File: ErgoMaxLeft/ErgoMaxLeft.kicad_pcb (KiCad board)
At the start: 2 copper layers, 92 parts, among them J1 AudioJack4_Ground, K1 KEYSW, K10 KEYSW, K11 KEYSW, K12 KEYSW, K13 KEYSW, K14 KEYSW, K15 KEYSW, K16 KEYSW, K17 KEYSW, K18 KEYSW, K19 KEYSW, K2 KEYSW, K20 KEYSW, K21 KEYSW, K22 KEYSW, K23 KEYSW, K24 KEYSW, K25 KEYSW, K26 KEYSW, K27 KEYSW, K28 KEYSW, K29 KEYSW, K3 KEYSW, K30 KEYSW, K31 KEYSW, K32 KEYSW, K33 KEYSW, K34 KEYSW, K35 KEYSW, K36 KEYSW, K37 KEYSW, K38 KEYSW, K39 KEYSW, K4 KEYSW, K40 KEYSW, K41 KEYSW, K42 KEYSW, K43 KEYSW, K44 KEYSW, K5 KEYSW, K6 KEYSW, K7 KEYSW, K8 KEYSW, K9 KEYSW, U1 ProMicro

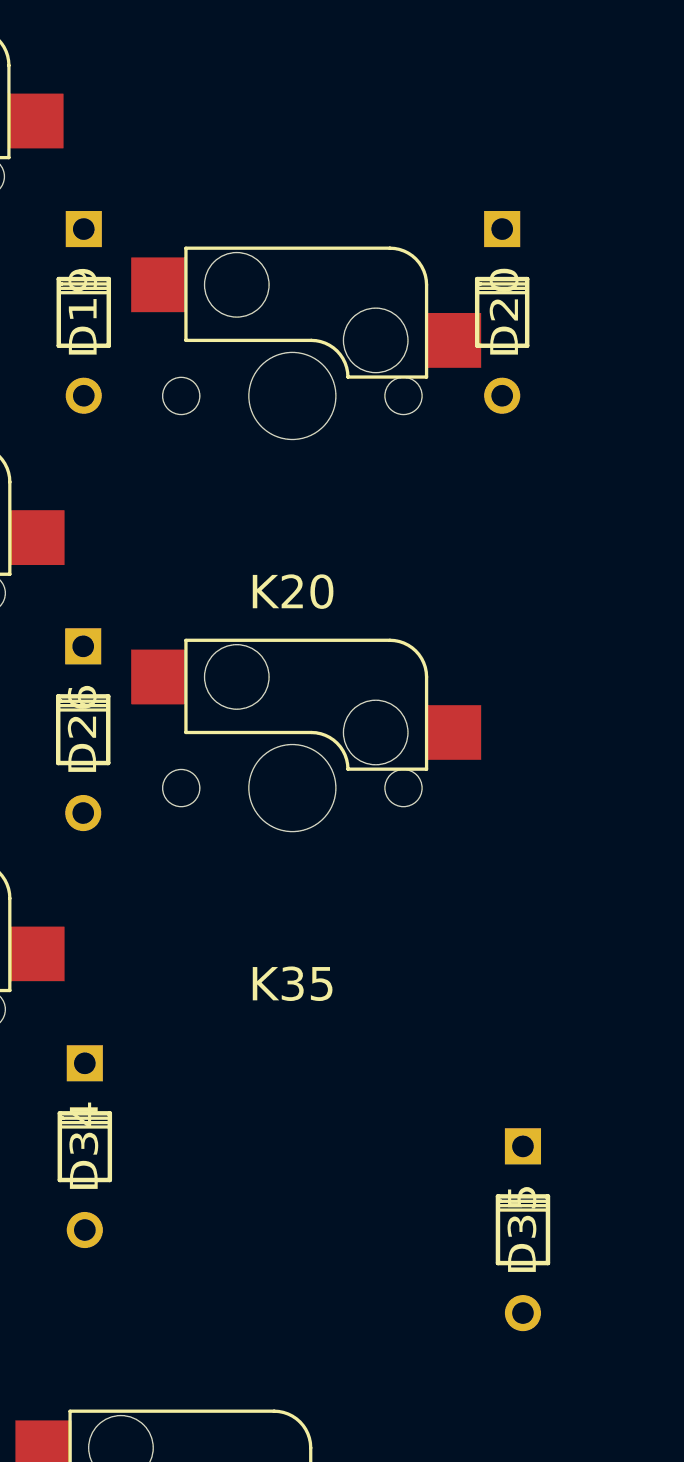
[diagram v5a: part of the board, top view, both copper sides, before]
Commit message: WIP PCB: fix spacing for the 2 1.5u keys on right side
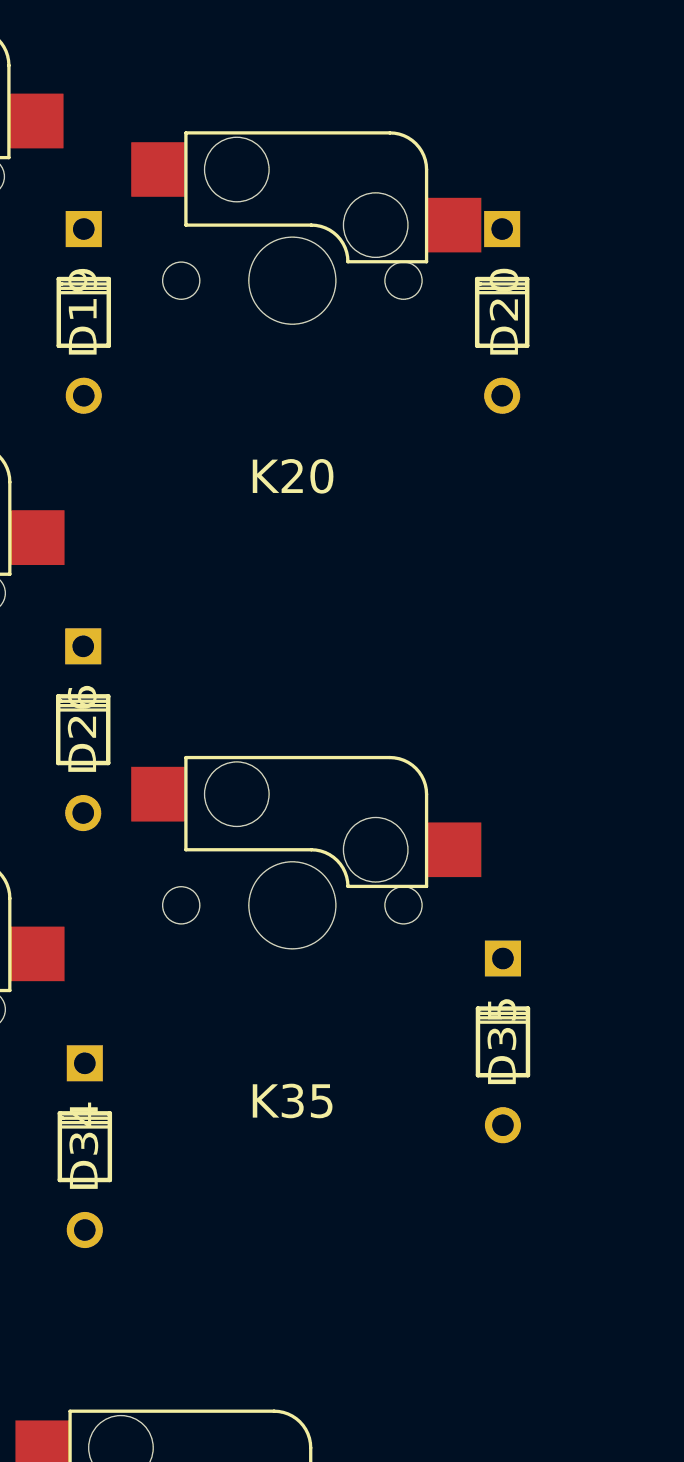
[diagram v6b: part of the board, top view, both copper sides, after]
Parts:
- moved D35 8.64 mm to (238.2, 102.8)
- moved K35 5.36 mm to (228.6, 96.6)
- moved K20 5.27 mm to (228.6, 68.0)
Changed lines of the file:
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@@
   )
   (module Keebio-Parts:Diode (layer F.Cu)
-    (at 239.141 111.4298 90)
+    (at 238.2266 102.84206 90)
     (fp_text reference D35 (at 0 0 90) (layer F.SilkS)
       (effects (font (size 1.27 1.524) (thickness 0.2032)))
@@
   )
   (module keyboard_parts:Kailh_MX_Socket (layer F.Cu)
-    (at 228.6 73.31564)
+    (at 228.6 68.04564)
     (fp_text reference K20 (at 0 9) (layer F.SilkS)
       (effects (font (size 1.524 1.524) (thickness 0.3048)))
@@
   )
   (module keyboard_parts:Kailh_MX_Socket (layer F.Cu)
-    (at 228.6 91.24)
+    (at 228.6 96.6)
     (fp_text reference K35 (at 0 9) (layer F.SilkS)
       (effects (font (size 1.524 1.524) (thickness 0.3048)))

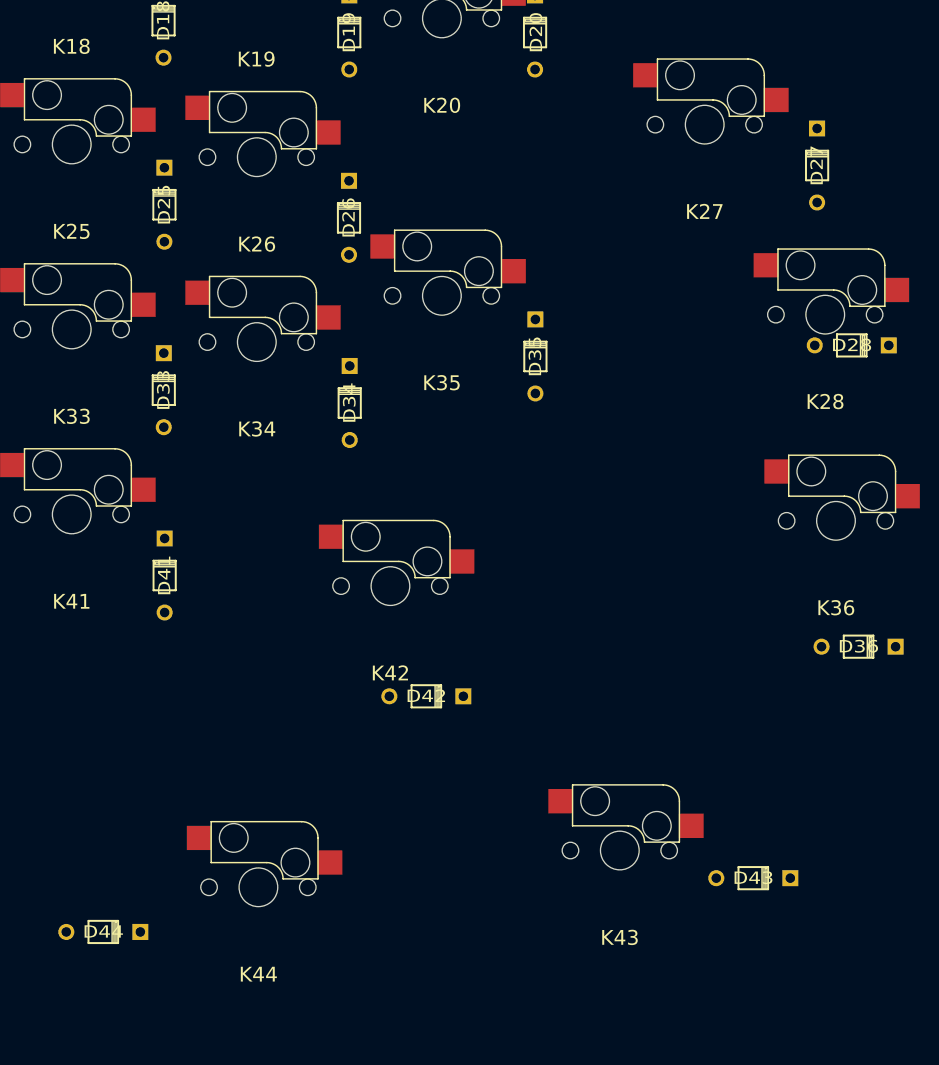
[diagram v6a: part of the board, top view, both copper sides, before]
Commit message: WIP PCB: place thumb switch sockets
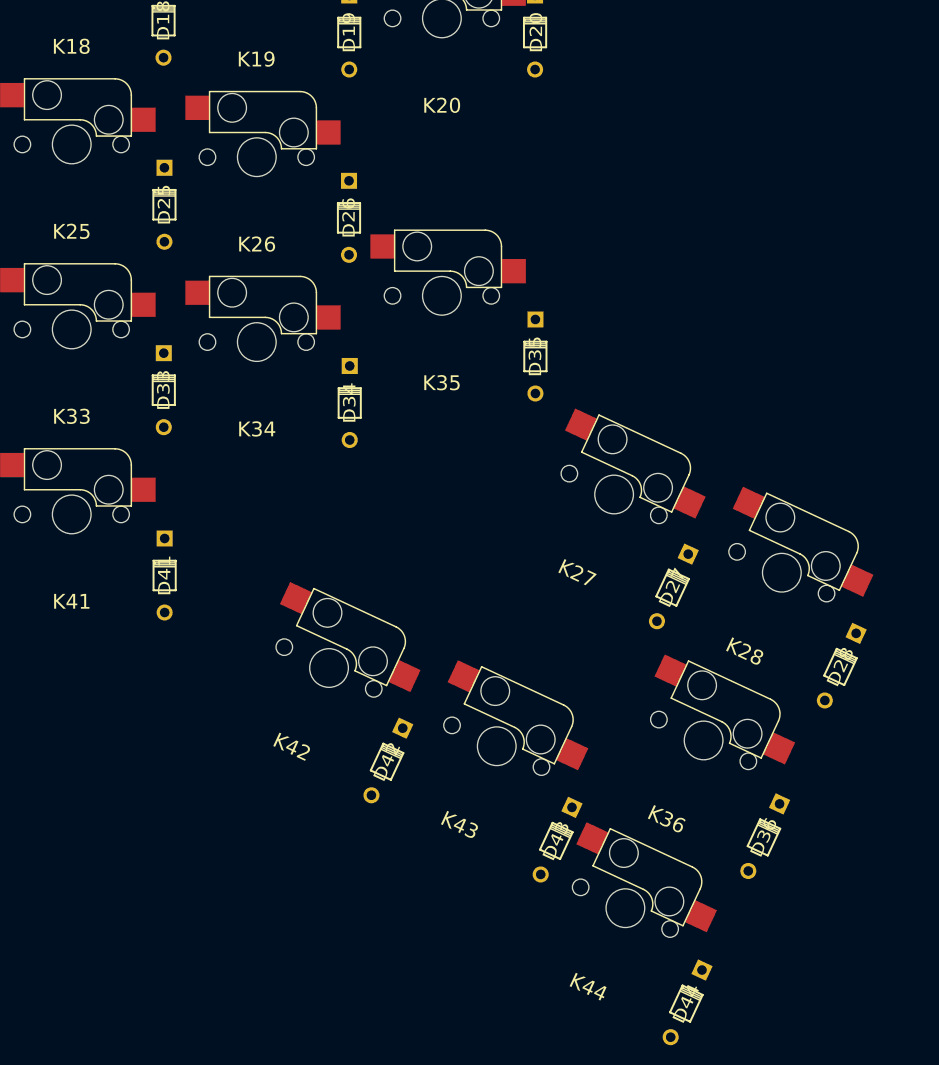
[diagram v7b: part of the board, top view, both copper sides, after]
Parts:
- moved D44 60.5 mm to (253.8, 169.5), turned to 65 degrees
- moved D27 45.9 mm to (252.3, 126.6), turned to 65 degrees
- moved K27 39.2 mm to (246.3, 117.0), turned to 335 degrees
- moved K44 37.8 mm to (247.5, 159.6), turned to 335 degrees
- moved D28 33.1 mm to (269.6, 134.8), turned to 65 degrees
- moved K28 26.9 mm to (263.6, 125.1), turned to 335 degrees
- moved K36 26.4 mm to (255.5, 142.4), turned to 335 degrees
- moved D36 21.9 mm to (261.7, 152.3), turned to 65 degrees
- moved D43 20.6 mm to (240.4, 152.7), turned to 65 degrees
- moved K43 16.6 mm to (234.2, 143.0), turned to 335 degrees
- moved K42 10.5 mm to (217.0, 134.9), turned to 335 degrees
- moved D42 7.86 mm to (223.0, 144.6), turned to 65 degrees

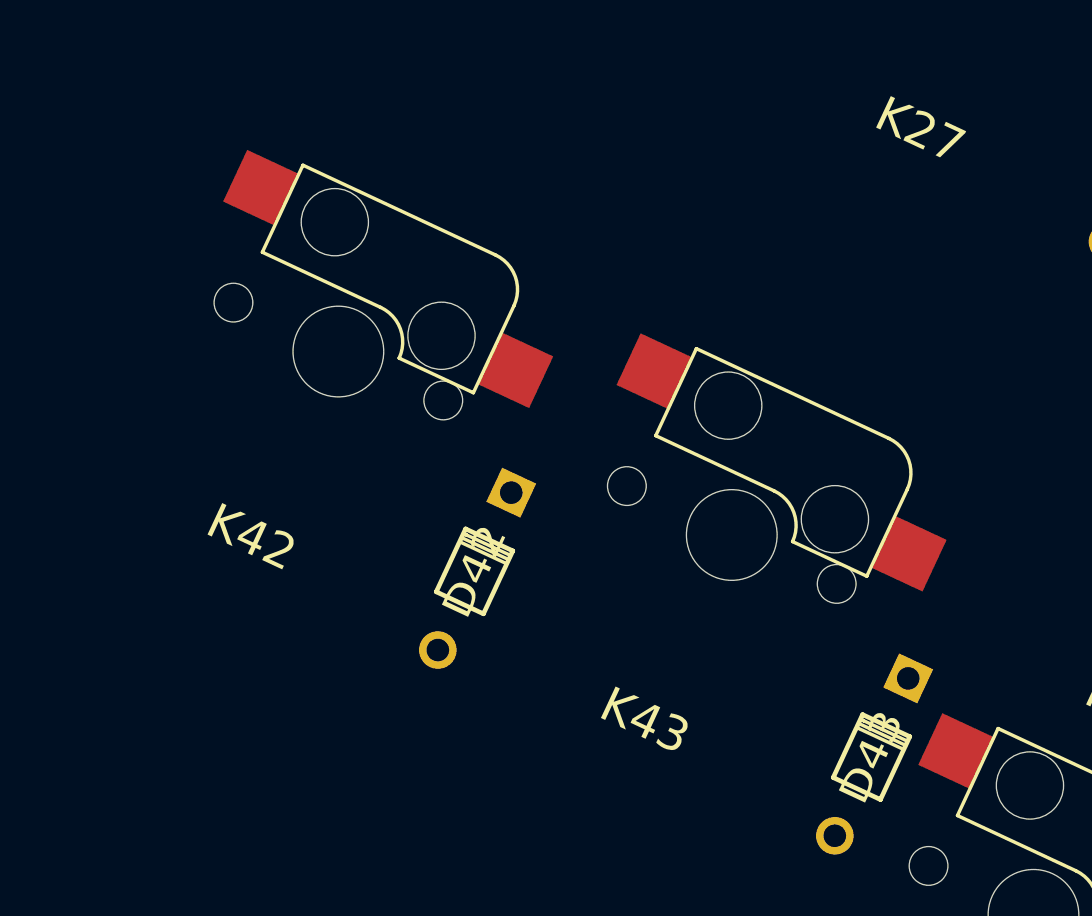
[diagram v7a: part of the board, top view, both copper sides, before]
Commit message: WIP PCB - rotate thumb 2u keys to be oriented properly for stabs
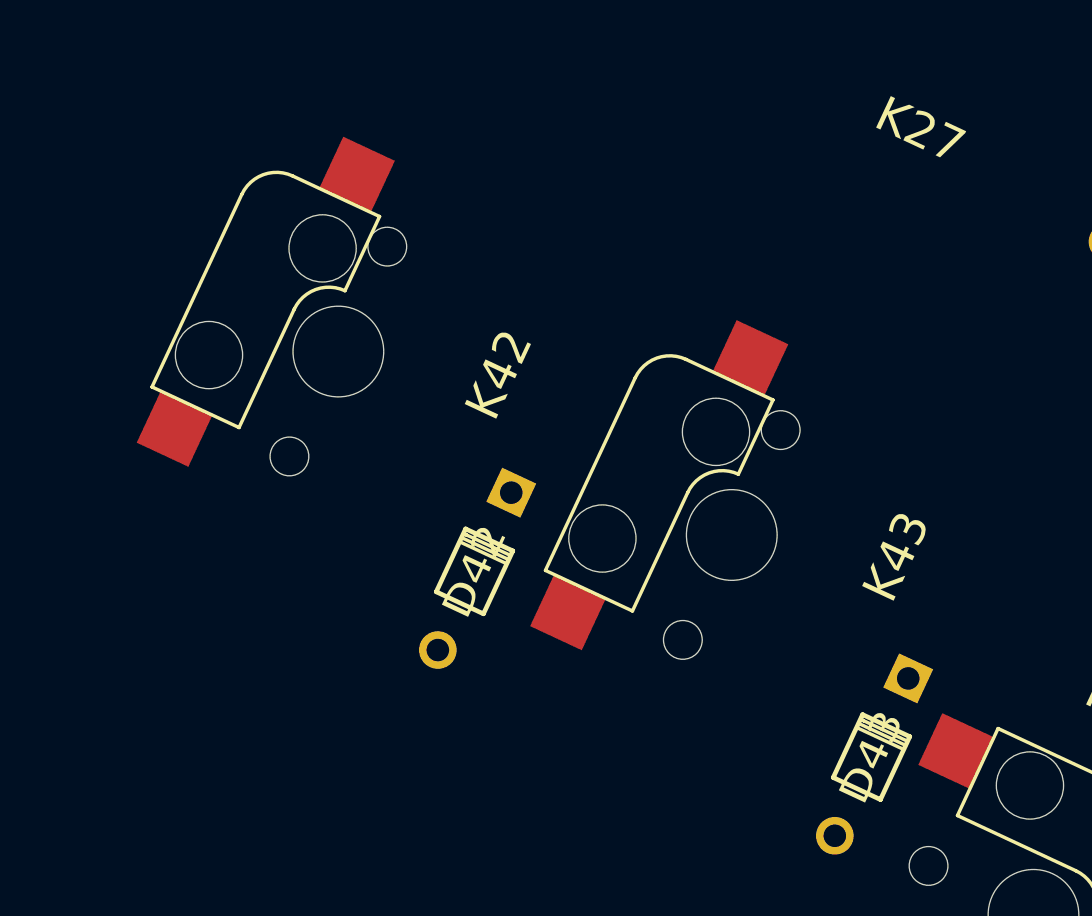
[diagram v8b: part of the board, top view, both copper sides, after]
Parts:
- turned K42 to 65 degrees
- turned K43 to 65 degrees
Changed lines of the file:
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@@
   )
   (module keyboard_parts:Kailh_MX_Socket (layer F.Cu)
-    (at 216.982334 134.909487 335)
-    (fp_text reference K42 (at 0 9 335) (layer F.SilkS)
+    (at 216.982334 134.909487 65)
+    (fp_text reference K42 (at 2.066879 6.818639 65) (layer F.SilkS)
       (effects (font (size 1.524 1.524) (thickness 0.3048)))
     )
-    (fp_text value KEYSW (at 0 7 335) (layer B.SilkS)
+    (fp_text value KEYSW (at 0 7 65) (layer B.SilkS)
       (effects (font (size 1.524 1.524) (thickness 0.3048)) (justify mirror))
     )
@@
     (fp_line (start -7.62 7.62) (end -5.62 7.62) (layer Dwgs.User) (width 0.381))
     (fp_line (start -7.62 -5.62) (end -7.62 -7.62) (layer Dwgs.User) (width 0.381))
-    (pad 1 smd rect (at 7.36 -2.54 335) (size 2.55 2.5) (layers F.Cu F.Paste F.Mask)
+    (pad 1 smd rect (at 7.36 -2.54 65) (size 2.55 2.5) (layers F.Cu F.Paste F.Mask)
       (net 50 "Net-(D42-Pad2)"))
-    (pad "" np_thru_hole circle (at 0 0 335) (size 3.98018 3.98018) (drill 3.98018) (layers *.Cu *.Mask))
-    (pad "" np_thru_hole circle (at -2.54 -5.08 335) (size 2.95 2.95) (drill 2.95) (layers *.Cu *.Mask))
-    (pad "" np_thru_hole circle (at 3.81 -2.54 335) (size 2.95 2.95) (drill 2.95) (layers *.Cu *.Mask))
-    (pad 2 smd rect (at -6.09 -5.08 335) (size 2.55 2.5) (layers F.Cu F.Paste F.Mask)
+    (pad "" np_thru_hole circle (at 0 0 65) (size 3.98018 3.98018) (drill 3.98018) (layers *.Cu *.Mask))
+    (pad "" np_thru_hole circle (at -2.54 -5.08 65) (size 2.95 2.95) (drill 2.95) (layers *.Cu *.Mask))
+    (pad "" np_thru_hole circle (at 3.81 -2.54 65) (size 2.95 2.95) (drill 2.95) (layers *.Cu *.Mask))
+    (pad 2 smd rect (at -6.09 -5.08 65) (size 2.55 2.5) (layers F.Cu F.Paste F.Mask)
       (net 58 /Row5))
-    (pad "" np_thru_hole circle (at -5.08 0 335) (size 1.7 1.7) (drill 1.7) (layers *.Cu *.Mask))
-    (pad "" np_thru_hole circle (at 5.08 0 335) (size 1.7 1.7) (drill 1.7) (layers *.Cu *.Mask))
+    (pad "" np_thru_hole circle (at -5.08 0 65) (size 1.7 1.7) (drill 1.7) (layers *.Cu *.Mask))
+    (pad "" np_thru_hole circle (at 5.08 0 65) (size 1.7 1.7) (drill 1.7) (layers *.Cu *.Mask))
     (model /Users/cole/git/keyboard_parts.pretty/PG151101S11.step
       (offset (xyz -4.65 6.8 1.8))
@@
   )
   (module keyboard_parts:Kailh_MX_Socket (layer F.Cu)
-    (at 234.247497 142.960364 335)
-    (fp_text reference K43 (at 0 9 335) (layer F.SilkS)
+    (at 234.247497 142.960364 65)
+    (fp_text reference K43 (at 2.19733 6.950322 65) (layer F.SilkS)
       (effects (font (size 1.524 1.524) (thickness 0.3048)))
     )
-    (fp_text value KEYSW (at 0 7 335) (layer B.SilkS)
+    (fp_text value KEYSW (at 0 7 65) (layer B.SilkS)
       (effects (font (size 1.524 1.524) (thickness 0.3048)) (justify mirror))
     )
@@
     (fp_line (start -7.62 7.62) (end -5.62 7.62) (layer Dwgs.User) (width 0.381))
     (fp_line (start -7.62 -5.62) (end -7.62 -7.62) (layer Dwgs.User) (width 0.381))
-    (pad 1 smd rect (at 7.36 -2.54 335) (size 2.55 2.5) (layers F.Cu F.Paste F.Mask)
+    (pad 1 smd rect (at 7.36 -2.54 65) (size 2.55 2.5) (layers F.Cu F.Paste F.Mask)
       (net 51 "Net-(D43-Pad2)"))
-    (pad "" np_thru_hole circle (at 0 0 335) (size 3.98018 3.98018) (drill 3.98018) (layers *.Cu *.Mask))
-    (pad "" np_thru_hole circle (at -2.54 -5.08 335) (size 2.95 2.95) (drill 2.95) (layers *.Cu *.Mask))
-    (pad "" np_thru_hole circle (at 3.81 -2.54 335) (size 2.95 2.95) (drill 2.95) (layers *.Cu *.Mask))
-    (pad 2 smd rect (at -6.09 -5.08 335) (size 2.55 2.5) (layers F.Cu F.Paste F.Mask)
+    (pad "" np_thru_hole circle (at 0 0 65) (size 3.98018 3.98018) (drill 3.98018) (layers *.Cu *.Mask))
+    (pad "" np_thru_hole circle (at -2.54 -5.08 65) (size 2.95 2.95) (drill 2.95) (layers *.Cu *.Mask))
+    (pad "" np_thru_hole circle (at 3.81 -2.54 65) (size 2.95 2.95) (drill 2.95) (layers *.Cu *.Mask))
+    (pad 2 smd rect (at -6.09 -5.08 65) (size 2.55 2.5) (layers F.Cu F.Paste F.Mask)
       (net 58 /Row5))
-    (pad "" np_thru_hole circle (at -5.08 0 335) (size 1.7 1.7) (drill 1.7) (layers *.Cu *.Mask))
-    (pad "" np_thru_hole circle (at 5.08 0 335) (size 1.7 1.7) (drill 1.7) (layers *.Cu *.Mask))
+    (pad "" np_thru_hole circle (at -5.08 0 65) (size 1.7 1.7) (drill 1.7) (layers *.Cu *.Mask))
+    (pad "" np_thru_hole circle (at 5.08 0 65) (size 1.7 1.7) (drill 1.7) (layers *.Cu *.Mask))
     (model /Users/cole/git/keyboard_parts.pretty/PG151101S11.step
       (offset (xyz -4.65 6.8 1.8))
